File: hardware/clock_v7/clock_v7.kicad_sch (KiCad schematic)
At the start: 151 parts, among them J1 RJ45, J12 Conn_01x06, J2 Conn_01x06_Pin, J4 Conn_01x04_Pin, J5 Conn_01x06_Pin, J6 Conn_01x04_Pin, J7 Conn_01x04_Pin, J8 Conn_01x02, Q10 2N7002, Q9 2N7002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

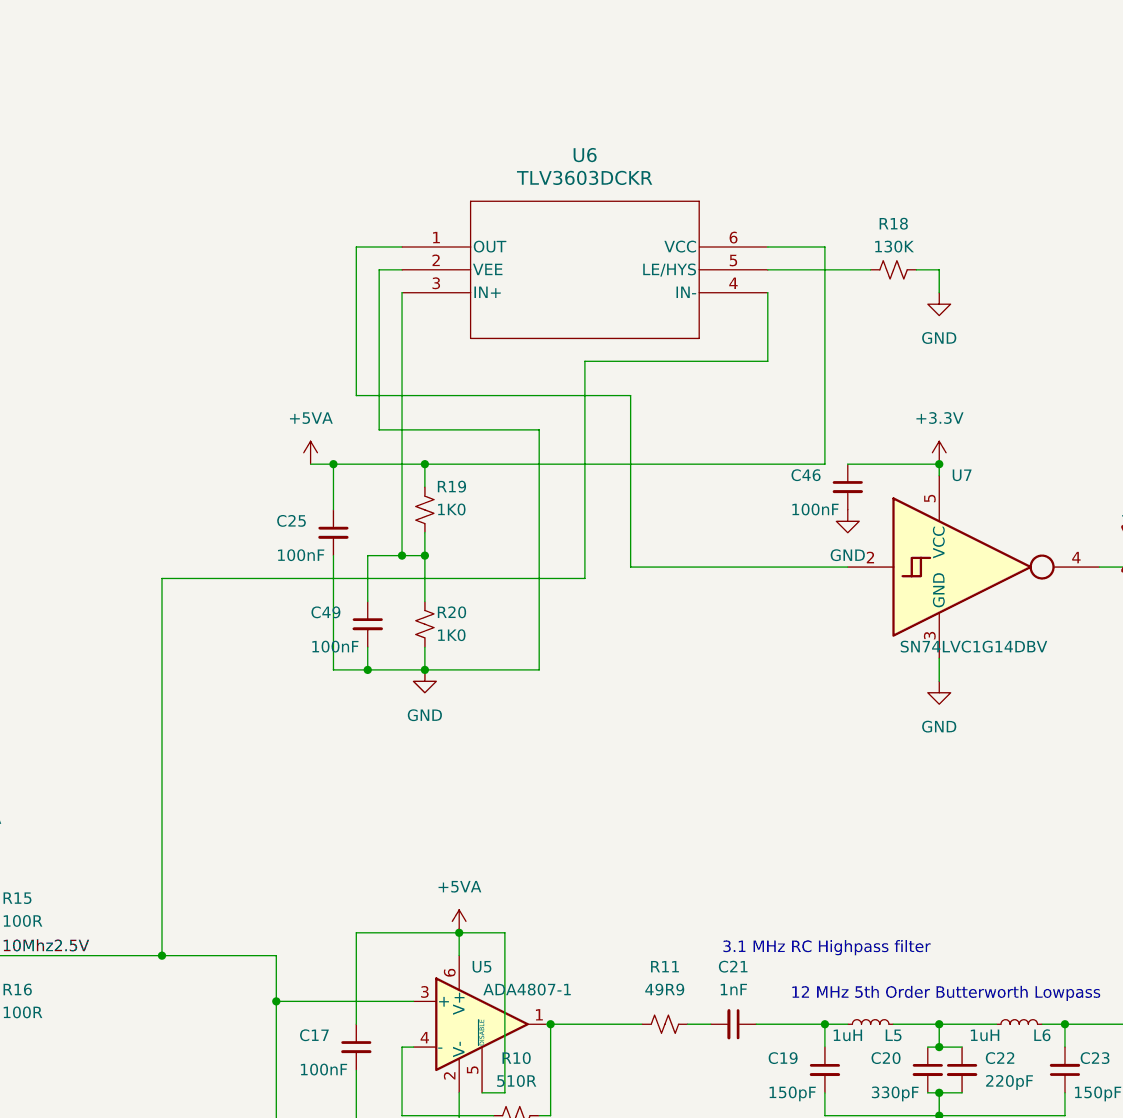
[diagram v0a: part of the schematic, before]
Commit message: update comparator symbol on schematic
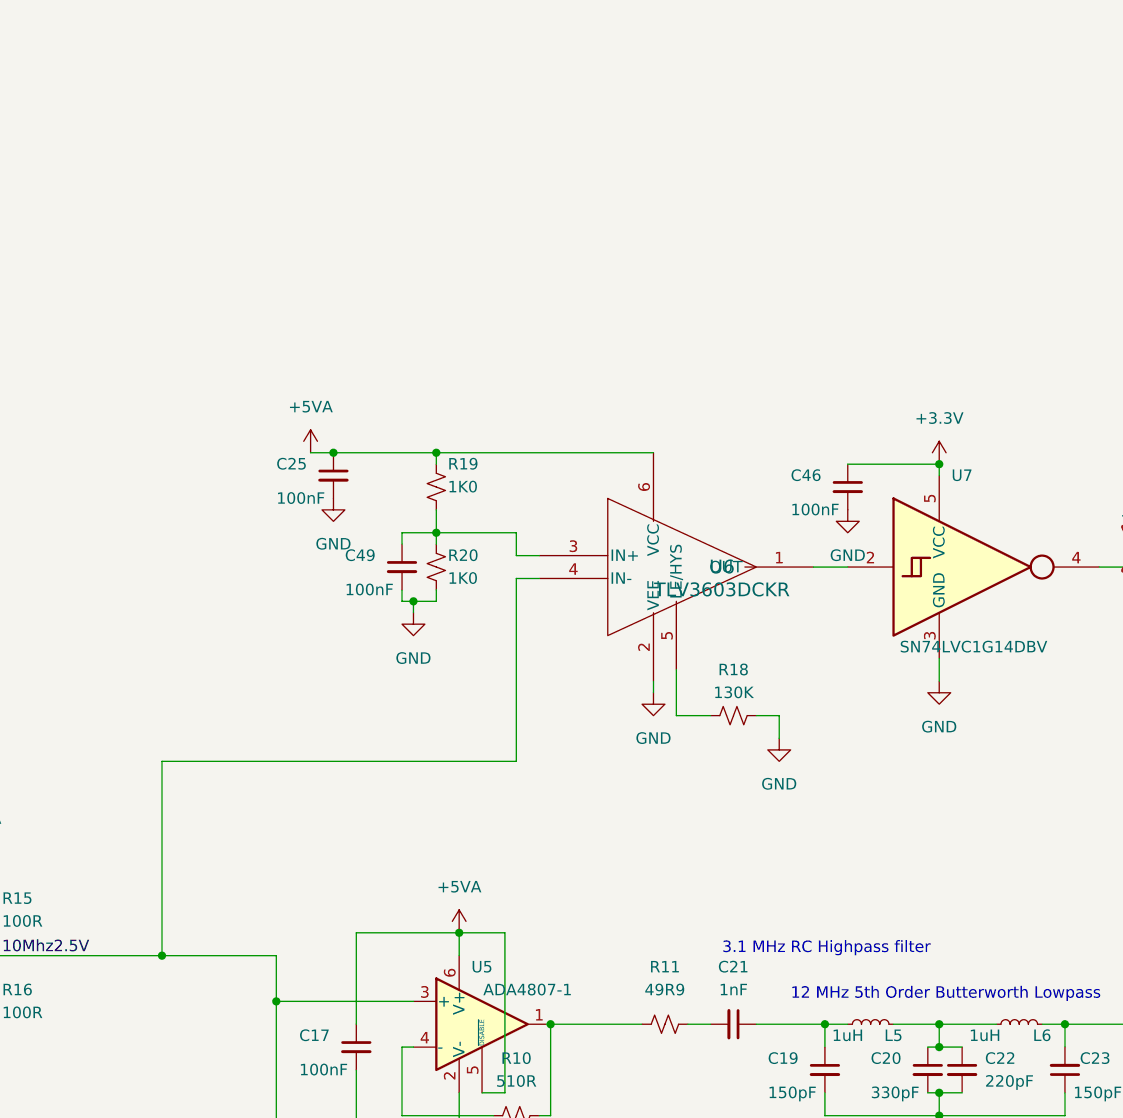
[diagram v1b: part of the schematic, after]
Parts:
- U6: footprint blinky_footprints:SC70_DCK_TEX -> SC70_DCK_TEX
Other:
- moved on the sheet: C25, C49, R18, R19, R20

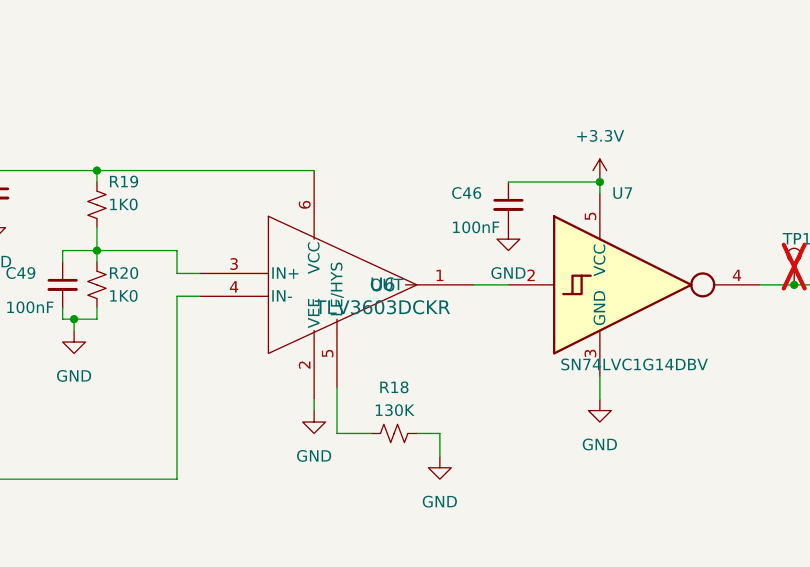
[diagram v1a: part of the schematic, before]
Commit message: update opamp symbol on clock board
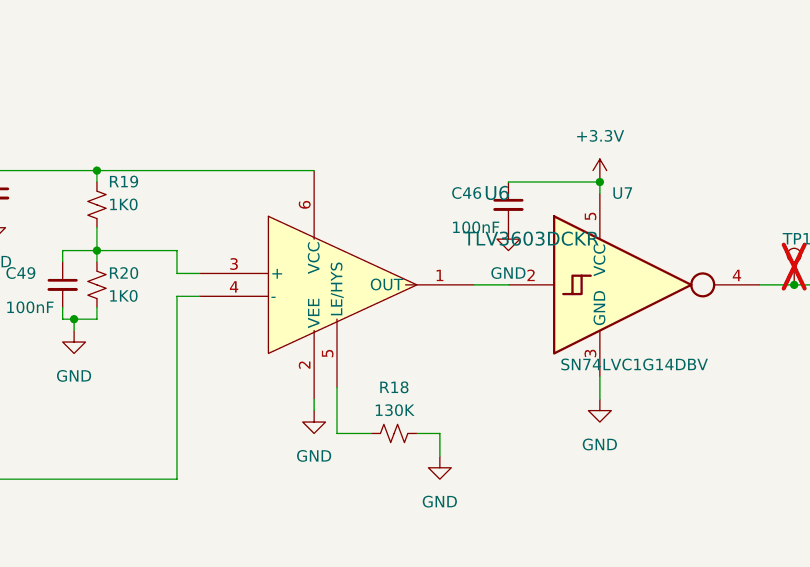
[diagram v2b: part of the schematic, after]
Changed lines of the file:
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@@
     )
   )
-  (symbol (lib_name "TLV3603DCKR_1") (lib_id "blinky:TLV3603DCKR") (at 332.74 87.63 0) (unit 1)
-    (in_bom yes) (on_board yes) (dnp no) (fields_autoplaced)
-    (property "Reference" "U6" (at 353.06 77.47 0)
+  (symbol (lib_name "TLV3603DCKR_1") (lib_id "blinky:TLV3603DCKR") (at 345.44 77.47 0) (unit 1)
+    (in_bom yes) (on_board yes) (dnp no)
+    (property "Reference" "U6" (at 365.76 67.31 0)
       (effects (font (size 1.524 1.524)))
     )
-    (property "Value" "TLV3603DCKR" (at 353.06 80.01 0)
+    (property "Value" "TLV3603DCKR" (at 369.57 72.39 0)
       (effects (font (size 1.524 1.524)))
     )
-    (property "Footprint" "SC70_DCK_TEX" (at 332.74 87.63 0)
+    (property "Footprint" "SC70_DCK_TEX" (at 345.44 77.47 0)
       (effects (font (size 1.27 1.27) italic) hide)
     )
-    (property "Datasheet" "TLV3603DCKR" (at 332.74 87.63 0)
+    (property "Datasheet" "TLV3603DCKR" (at 345.44 77.47 0)
       (effects (font (size 1.27 1.27) italic) hide)
     )
-    (property "LCSC" "" (at 332.74 87.63 0)
+    (property "LCSC" "" (at 345.44 77.47 0)
       (effects (font (size 1.27 1.27)) hide)
     )
-    (property "JLCPCB Part #" "C5213955" (at 332.74 87.63 0)
+    (property "JLCPCB Part #" "C5213955" (at 345.44 77.47 0)
       (effects (font (size 1.27 1.27)) hide)
     )
     (pin "1")
     (pin "2")
+    (pin "5")
+    (pin "6")
     (pin "3")
     (pin "4")
-    (pin "5")
-    (pin "6")
     (instances
       (project "clock_v7"

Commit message: clean up symbols
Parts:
- C1, C10, C11, C17, C18, C2, C24, C25, C26, C27, C30, C31, C32, C33, C36, C37, C38, C39, C45, C46, C47, C48, C49, C9: value 100nF -> 100n
- C12, C14, C19, C23, C5, C7: value 150pF -> 150p
- C13, C20, C8: value 330pF -> 330p
- C15, C22, C6: value 220pF -> 220p
- C16, C21, C3: value 1nF -> 1n0
- C28, C29: value 33pF -> 33p
- C34, C41, C43: value 10uF -> 10u
- C35, C40: value 2.2uF -> 2u2
- C4: value 47pF -> 47p
- C42, C44: value 33uF -> 33u
- J? (x5): MPN KH-BNC50-3511 -> (none)
- S1, S2: Comment 147873-2 -> (none); Configuration_Pole-Throw Single Pole - Single Throw -> (none); Contact_Current_Rating 50 mA -> (none)
- U12: MAXIMUM_PACKAGE_HEIGHT 2.005 mm -> (none); PARTREV 003 -> (none); STANDARD IPC 7351B -> (none)
- Y1: MAXIMUM_PACKAGE_HEIGHT 13.76 mm -> (none); PARTREV 07.24.11 -> (none); SNAPEDA_PN AOCJY4A-10.000MHZ-SW -> (none); STANDARD IPC_7351B -> (none)
